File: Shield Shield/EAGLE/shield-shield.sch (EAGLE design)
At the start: 23 parts, among them IC1 MC33269D-5.0, J1 POWER_JACKSLT, U1 TXB0108PWR, U2 TXB0108PWR

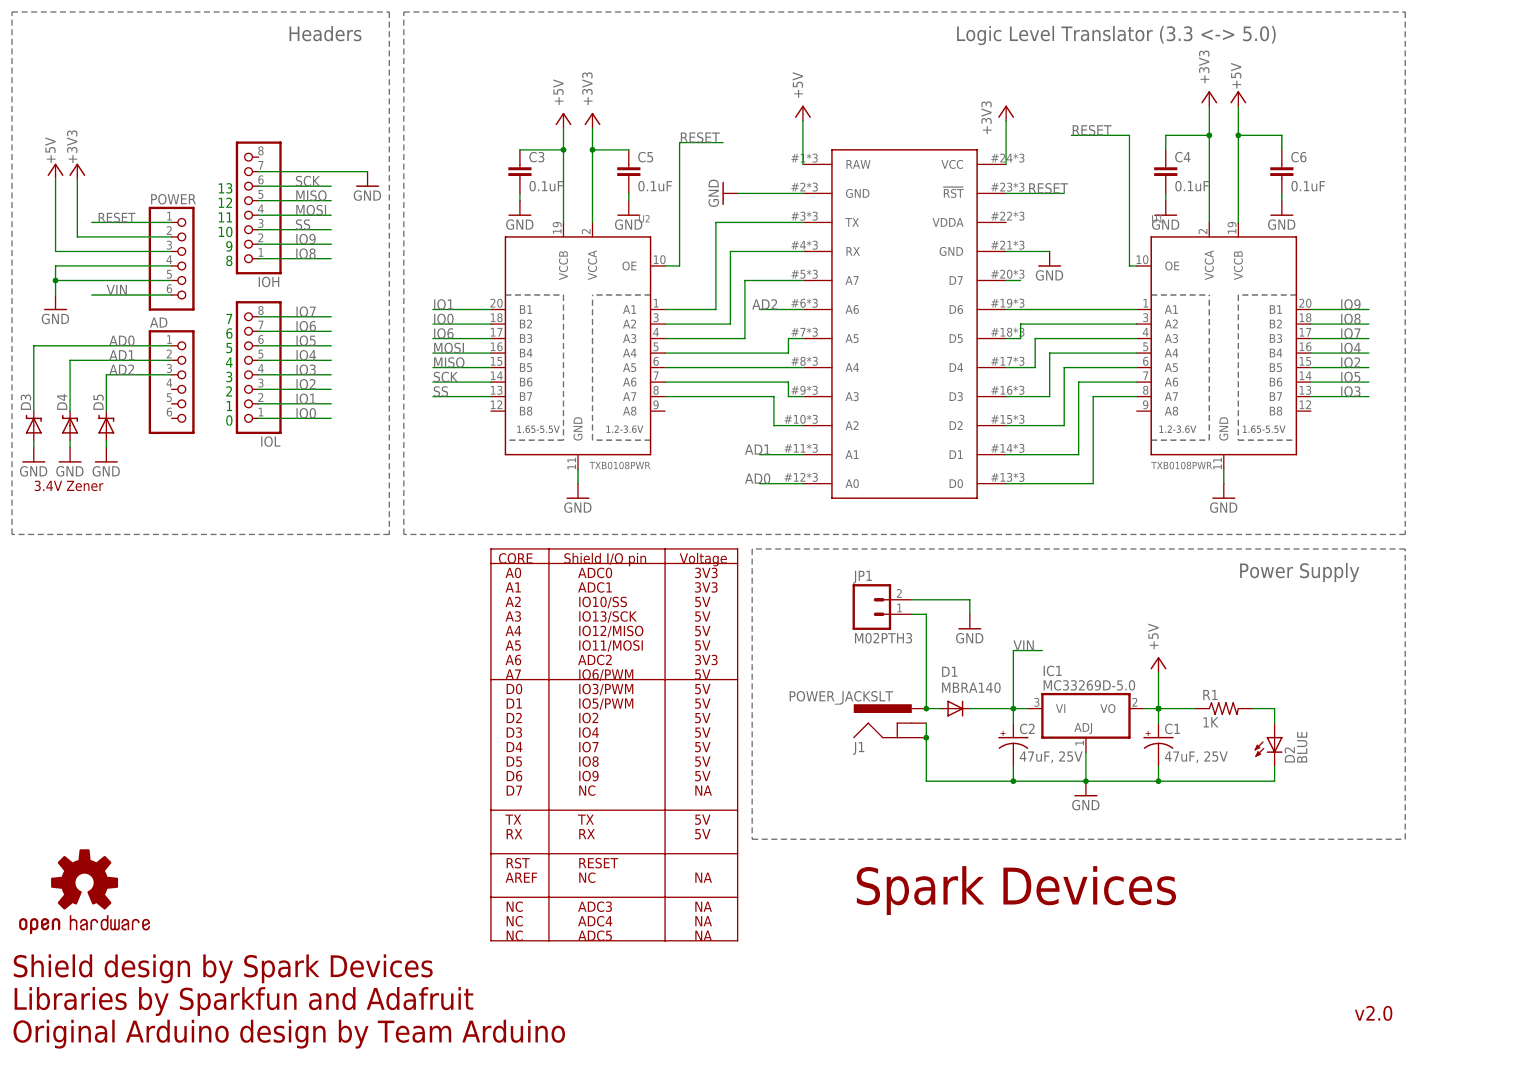
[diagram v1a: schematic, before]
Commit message: added resistors to the sshield and some minor edits
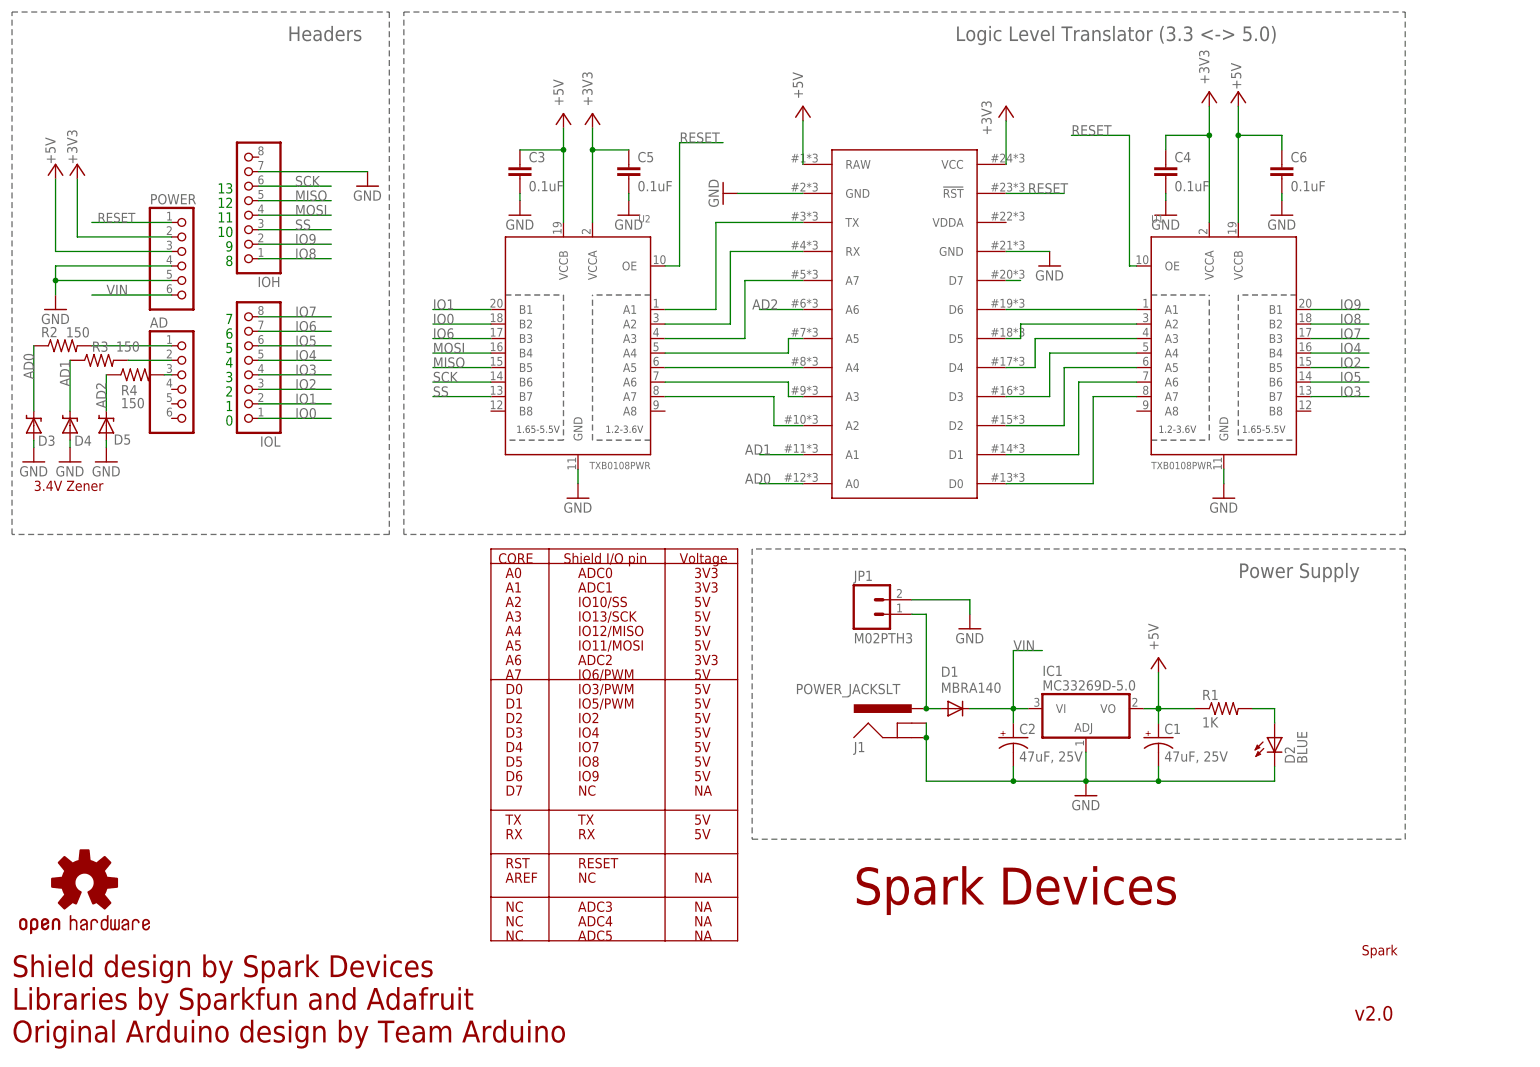
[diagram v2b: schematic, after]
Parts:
- added R2, R3, R4: 150, SparkFun-Passives:RESISTOR0603-RES
- added U$3: SPARK_LOGO, Spark:SPARK_LOGO
- J1: device SparkFun-Connectors:POWER_JACKSLT -> Spark:POWER_JACKSLT
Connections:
- new net N$10: AD.1, R2.2
- new net N$11: AD.2, R3.2
- new net N$12: AD.3, R4.2
- net AD0: now also R2.1; no longer AD.1
- net AD1: now also R3.1; no longer AD.2
- net AD2: now also R4.1; no longer AD.3
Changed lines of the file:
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@@
 <setting verticaltext="up"/>
 </settings>
-<grid distance="0.05" unitdist="inch" unit="inch" style="lines" multiple="1" display="yes" altdistance="0.01" altunitdist="inch" altunit="inch"/>
+<grid distance="0.1" unitdist="inch" unit="inch" style="lines" multiple="1" display="no" altdistance="0.01" altunitdist="inch" altunit="inch"/>
 <layers>
 <layer number="1" name="Top" color="4" fill="1" visible="no" active="no"/>
@@
 <part name="GND5" library="supply1" deviceset="GND" device=""/>
 <part name="GND6" library="supply1" deviceset="GND" device=""/>
-<part name="J1" library="SparkFun-Connectors" deviceset="POWER_JACK" device="SLT"/>
 <part name="GND7" library="supply1" deviceset="GND" device=""/>
 <part name="+3V7" library="supply1" deviceset="+3V3" device=""/>
@@
 <part name="GND13" library="supply1" deviceset="GND" device=""/>
 <part name="GND15" library="supply1" deviceset="GND" device=""/>
+<part name="R2" library="SparkFun-Passives" deviceset="RESISTOR" device="0603-RES" value="150"/>
+<part name="R3" library="SparkFun-Passives" deviceset="RESISTOR" device="0603-RES" value="150"/>
+<part name="R4" library="SparkFun-Passives" deviceset="RESISTOR" device="0603-RES" value="150"/>
+<part name="J1" library="Spark" deviceset="POWER_JACK" device="SLT"/>
+<part name="U$3" library="Spark" deviceset="SPARK_LOGO" device=""/>
 </parts>
 <sheets>
@@
 <instance part="GND5" gate="1" x="110.49" y="147.32"/>
 <instance part="GND6" gate="1" x="224.79" y="147.32"/>
-<instance part="J1" gate="G$1" x="160.02" y="53.34" smashed="yes">
-<attribute name="VALUE" x="138.43" y="62.23" size="1.778" layer="96" font="vector"/>
-<attribute name="NAME" x="149.86" y="53.34" size="1.778" layer="95"/>
-</instance>
 <instance part="GND7" gate="1" x="190.5" y="45.72"/>
 <instance part="+3V7" gate="G$1" x="176.53" y="166.37"/>
@@
 <instance part="LOGO1" gate="G$1" x="15.24" y="30.48"/>
 <instance part="D3" gate="G$1" x="6.35" y="110.49" smashed="yes" rot="R90">
-<attribute name="NAME" x="5.8674" y="113.03" size="1.778" layer="95" rot="R90"/>
+<attribute name="NAME" x="10.16" y="108.7374" size="1.778" layer="95" rot="R180"/>
 <attribute name="VALUE" x="8.6614" y="113.03" size="1.778" layer="96" rot="R90" display="off"/>
 </instance>
 <instance part="D4" gate="G$1" x="12.7" y="110.49" smashed="yes" rot="R90">
-<attribute name="NAME" x="12.2174" y="113.03" size="1.778" layer="95" rot="R90"/>
+<attribute name="NAME" x="16.51" y="108.7374" size="1.778" layer="95" rot="R180"/>
 <attribute name="VALUE" x="15.0114" y="113.03" size="1.778" layer="96" rot="R90" display="off"/>
 </instance>
 <instance part="D5" gate="G$1" x="19.05" y="110.49" smashed="yes" rot="R90">
-<attribute name="NAME" x="18.5674" y="113.03" size="1.778" layer="95" rot="R90"/>
+<attribute name="NAME" x="20.32" y="107.1626" size="1.778" layer="95"/>
 <attribute name="VALUE" x="21.3614" y="113.03" size="1.778" layer="96" rot="R90" display="off"/>
 </instance>
@@
 <instance part="GND13" gate="1" x="12.7" y="104.14"/>
 <instance part="GND15" gate="1" x="6.35" y="104.14"/>
+<instance part="R2" gate="G$1" x="11.43" y="124.46" smashed="yes">
+<attribute name="NAME" x="7.62" y="125.9586" size="1.778" layer="95"/>
+<attribute name="VALUE" x="11.9634" y="125.9332" size="1.778" layer="96"/>
+</instance>
+<instance part="R3" gate="G$1" x="17.78" y="121.92" smashed="yes">
+<attribute name="NAME" x="16.51" y="123.4186" size="1.778" layer="95"/>
+<attribute name="VALUE" x="20.7264" y="123.444" size="1.778" layer="96"/>
+</instance>
+<instance part="R4" gate="G$1" x="24.13" y="119.38" smashed="yes">
+<attribute name="NAME" x="21.59" y="115.7986" size="1.778" layer="95"/>
+<attribute name="VALUE" x="21.59" y="113.538" size="1.778" layer="96"/>
+</instance>
+<instance part="J1" gate="G$1" x="160.02" y="53.34" smashed="yes">
+<attribute name="VALUE" x="139.7" y="63.5" size="1.778" layer="96"/>
+<attribute name="NAME" x="149.86" y="53.34" size="1.778" layer="95"/>
+</instance>
+<instance part="U$3" gate="G$1" x="238.76" y="17.78"/>
 </instances>
 <busses>
@@
 <junction x="190.5" y="48.26"/>
 <pinref part="GND7" gate="1" pin="GND"/>
-<pinref part="J1" gate="G$1" pin="GNDBREAK"/>
-<pinref part="J1" gate="G$1" pin="GND"/>
 <wire x1="162.56" y1="58.42" x2="162.56" y2="55.88" width="0.2032" layer="91"/>
 <wire x1="162.56" y1="55.88" x2="162.56" y2="48.26" width="0.1524" layer="91"/>
-<junction x="162.56" y="55.88"/>
 <wire x1="162.56" y1="48.26" x2="177.8" y2="48.26" width="0.1524" layer="91"/>
 <junction x="177.8" y="48.26"/>
@@
 <wire x1="223.52" y1="48.26" x2="203.2" y2="48.26" width="0.1524" layer="91"/>
 <junction x="203.2" y="48.26"/>
+<pinref part="J1" gate="G$1" pin="GNDBREAK"/>
+<pinref part="J1" gate="G$1" pin="GND"/>
+<junction x="162.56" y="55.88"/>
 </segment>
 <segment>
@@
 <net name="AD0" class="0">
 <segment>
-<wire x1="30.48" y1="124.46" x2="6.35" y2="124.46" width="0.1524" layer="91"/>
-<label x="24.13" y="124.46" size="1.778" layer="95" rot="MR0"/>
-<pinref part="AD" gate="A" pin="1"/>
+<label x="6.35" y="123.19" size="1.778" layer="95" rot="MR270"/>
 <pinref part="D3" gate="G$1" pin="C"/>
 <wire x1="6.35" y1="124.46" x2="6.35" y2="113.03" width="0.1524" layer="91"/>
+<pinref part="R2" gate="G$1" pin="1"/>
 </segment>
 <segment>
@@
 <net name="AD1" class="0">
 <segment>
-<label x="24.13" y="121.92" size="1.778" layer="95" rot="MR0"/>
-<pinref part="AD" gate="A" pin="2"/>
-<wire x1="12.7" y1="121.92" x2="30.48" y2="121.92" width="0.1524" layer="91"/>
+<label x="12.7" y="121.92" size="1.778" layer="95" rot="MR270"/>
 <pinref part="D4" gate="G$1" pin="C"/>
 <wire x1="12.7" y1="121.92" x2="12.7" y2="113.03" width="0.1524" layer="91"/>
+<pinref part="R3" gate="G$1" pin="1"/>
 </segment>
 <segment>
@@
 <net name="AD2" class="0">
 <segment>
-<wire x1="30.48" y1="119.38" x2="19.05" y2="119.38" width="0.1524" layer="91"/>
-<label x="24.13" y="119.38" size="1.778" layer="95" rot="MR0"/>
-<pinref part="AD" gate="A" pin="3"/>
+<label x="19.05" y="118.11" size="1.778" layer="95" rot="MR270"/>
 <pinref part="D5" gate="G$1" pin="C"/>
 <wire x1="19.05" y1="119.38" x2="19.05" y2="113.03" width="0.1524" layer="91"/>
+<pinref part="R4" gate="G$1" pin="1"/>
 </segment>
 <segment>
@@
 <net name="N$8" class="0">
 <segment>
-<pinref part="J1" gate="G$1" pin="PWR"/>
 <pinref part="D1" gate="G$1" pin="A"/>
 <wire x1="162.56" y1="60.96" x2="165.1" y2="60.96" width="0.1524" layer="91"/>
@@
 <wire x1="160.02" y1="77.47" x2="162.56" y2="77.47" width="0.1524" layer="91"/>
 <wire x1="162.56" y1="77.47" x2="162.56" y2="60.96" width="0.1524" layer="91"/>
+<pinref part="J1" gate="G$1" pin="PWR"/>
 <junction x="162.56" y="60.96"/>
 </segment>
@@
 </segment>
 </net>
+<net name="N$10" class="0">
+<segment>
+<pinref part="R2" gate="G$1" pin="2"/>
+<pinref part="AD" gate="A" pin="1"/>
+<wire x1="16.51" y1="124.46" x2="30.48" y2="124.46" width="0.1524" layer="91"/>
+</segment>
+</net>
+<net name="N$11" class="0">
+<segment>
+<pinref part="R3" gate="G$1" pin="2"/>
+<pinref part="AD" gate="A" pin="2"/>
+<wire x1="22.86" y1="121.92" x2="30.48" y2="121.92" width="0.1524" layer="91"/>
+</segment>
+</net>
+<net name="N$12" class="0">
+<segment>
+<pinref part="R4" gate="G$1" pin="2"/>
+<pinref part="AD" gate="A" pin="3"/>
+<wire x1="29.21" y1="119.38" x2="30.48" y2="119.38" width="0.1524" layer="91"/>
+</segment>
+</net>

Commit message: added license info to all design files
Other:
- note added: "Reference Designs ARE PROVIDED "AS IS" AND "WITH ALL FAULTS. SPARK LABS, INC ("SPARK") DISCLAIMS ALL OTHER WARRANTIES, EXPRESS OR IMPLIED, REGARDING PRODUCTS OR THE REFERENCE DESIGNS, INCLUDING BUT NOT LIMITED TO, ANY IMPLIED WARRANTIES OF MERCHANTABILITY, FITNESS FOR A PARTICULAR PURPOSE, OR NON-INFRINGEMENT. Spark may make changes to specifications and product descriptions at any time, without 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"
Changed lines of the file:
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@@
 <setting verticaltext="up"/>
 </settings>
-<grid distance="0.1" unitdist="inch" unit="inch" style="lines" multiple="1" display="no" altdistance="0.01" altunitdist="inch" altunit="inch"/>
+<grid distance="0.1" unitdist="inch" unit="inch" style="lines" multiple="1" display="yes" altdistance="0.01" altunitdist="inch" altunit="inch"/>
 <layers>
 <layer number="1" name="Top" color="4" fill="1" visible="no" active="no"/>
@@
 <text x="6.35" y="99.06" size="1.778" layer="94" font="vector">3.4V Zener</text>
 <text x="237.49" y="6.35" size="2.54" layer="94" font="vector">v2.0</text>
+<text x="5.08" y="48.26" size="1.27" layer="95">Reference Designs ARE PROVIDED "AS IS" AND "WITH ALL FAULTS. SPARK LABS, INC
+("SPARK") DISCLAIMS ALL OTHER WARRANTIES, EXPRESS OR IMPLIED, REGARDING
+PRODUCTS OR THE REFERENCE DESIGNS, INCLUDING BUT NOT LIMITED TO, ANY
+IMPLIED WARRANTIES OF MERCHANTABILITY, FITNESS FOR A PARTICULAR PURPOSE,
+ OR NON-INFRINGEMENT.
+Spark may make changes to specifications and product descriptions at any
+time, without notice. The Customer must not rely on the absence or
+characteristics of any features or instructions marked "reserved" or
+"undefined." Spark reserves these for future definition and shall have
+no responsibility whatsoever for conflicts or incompatibilities arising
+from future changes to them. The product information on the Web Site or
+Materials is subject to change without notice. Do not finalize a design
+with this information.
+Spark is a registered trademark.</text>
+<wire x1="2.54" y1="83.82" x2="83.82" y2="83.82" width="0.2032" layer="95" style="shortdash"/>
+<wire x1="83.82" y1="83.82" x2="83.82" y2="40.64" width="0.2032" layer="95" style="shortdash"/>
+<wire x1="83.82" y1="40.64" x2="2.54" y2="40.64" width="0.2032" layer="95" style="shortdash"/>
+<wire x1="2.54" y1="40.64" x2="2.54" y2="83.82" width="0.2032" layer="95" style="shortdash"/>
 </plain>
 <instances>

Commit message: updated sshield and pshield gerbers
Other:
- note added: "v2.0.1"
- note removed: "v2.0"
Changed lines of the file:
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@@
 <?xml version="1.0" encoding="utf-8"?>
 <!DOCTYPE eagle SYSTEM "eagle.dtd">
-<eagle version="6.3">
+<eagle version="6.5.0">
 <drawing>
 <settings>
@@
 <setting verticaltext="up"/>
 </settings>
-<grid distance="0.1" unitdist="inch" unit="inch" style="lines" multiple="1" display="yes" altdistance="0.01" altunitdist="inch" altunit="inch"/>
+<grid distance="0.1" unitdist="inch" unit="inch" style="lines" multiple="1" display="no" altdistance="0.01" altunitdist="inch" altunit="inch"/>
 <layers>
 <layer number="1" name="Top" color="4" fill="1" visible="no" active="no"/>
@@
 <wire x1="86.36" y1="27.94" x2="129.54" y2="27.94" width="0.2032" layer="94"/>
 <text x="6.35" y="99.06" size="1.778" layer="94" font="vector">3.4V Zener</text>
-<text x="237.49" y="6.35" size="2.54" layer="94" font="vector">v2.0</text>
+<text x="237.49" y="6.35" size="2.54" layer="94" font="vector">v2.0.1</text>
 <text x="5.08" y="48.26" size="1.27" layer="95">Reference Designs ARE PROVIDED "AS IS" AND "WITH ALL FAULTS. SPARK LABS, INC
 ("SPARK") DISCLAIMS ALL OTHER WARRANTIES, EXPRESS OR IMPLIED, REGARDING
